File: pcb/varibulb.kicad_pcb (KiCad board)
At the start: 2 copper layers, 53.8 x 53.8 mm, 44 parts, among them IC1 ATTINY2313A-P, P1 MAINS LIVE, P2 MAINS LIVE, P3 LAMP 1, P4 LAMP 2, P5 MAINS GROUND, P6 ISP, P7 COMM, SW1 ENCODER, U1 TRIAC, U2 TRIAC, U3 LDO 5V, X1 10MHz

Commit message: arrange some components
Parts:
- R1, R2, R6: footprint Resistors_ThroughHole:Resistor_Horizontal_RM15mm -> Resistors_ThroughHole:Resistor_Horizontal_RM10mm
- U3: footprint Housings_TO-92:TO-92-Free-molded-narrow -> Housings_TO-92:TO-92-Free-molded-wide
- moved U2 139.0 mm to (61.7, 125.7), turned to 120 degrees
- moved D2 124.2 mm to (27.9, 80.5), turned to 45 degrees
- moved D4 102.5 mm to (50.3, 115.6), turned to 270 degrees
- moved P5 99.9 mm to (74.4, 145.0)
- moved R6 90.4 mm to (57.4, 128.0), turned to 300 degrees
- moved D5 84.3 mm to (47.0, 118.1), turned to 82 degrees
- moved R5 80.9 mm to (71.4, 133.6)
- moved D6 67.8 mm to (53.3, 115.6), turned to 270 degrees
- moved C1 67.5 mm to (84.6, 133.9), turned to 180 degrees
- moved D1 55.5 mm to (87.6, 122.2)
- moved C5 54.1 mm to (59.9, 114.8)
- moved D3 49.4 mm to (87.1, 126.7)
- moved R1 46.8 mm to (89.7, 135.6), turned to 55 degrees
- moved R2 46.3 mm to (81.8, 130.0), turned to 180 degrees
- moved R3 40.3 mm to (101.9, 119.4), turned to 270 degrees
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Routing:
- net GND: track 0.00 -> 61.4 mm
- net Net-(P4-Pad1): track 0.00 -> 21.0 mm
- net Net-(C5-Pad1): track 0.00 -> 17.5 mm
- net Net-(F1-Pad2): track 0.00 -> 16.7 mm
- net Net-(C3-Pad1): track 0.00 -> 16.0 mm
- net /SENSE: track 0.00 -> 14.3 mm
- net Net-(F1-Pad1): track 0.00 -> 12.5 mm
- net Net-(C3-Pad2): track 0.00 -> 10.5 mm
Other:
- net class Default: clearance 0.2 -> 0.1; trace_width 0.25 -> 0.8; via_dia 0.6 -> 2.2; via_drill 0.4 -> 0.8
- rule trace_clearance: 0.2 -> 0.1

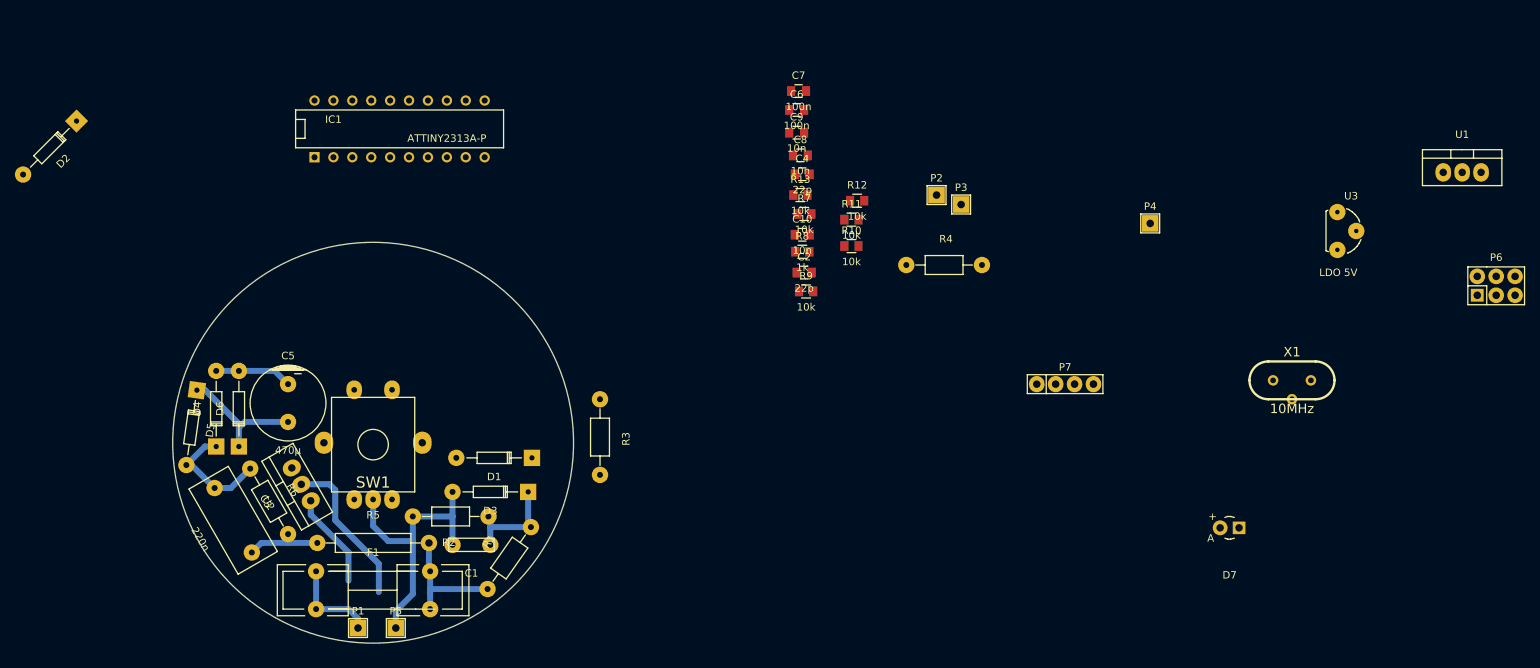
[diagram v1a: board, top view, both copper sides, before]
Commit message: arrange more components
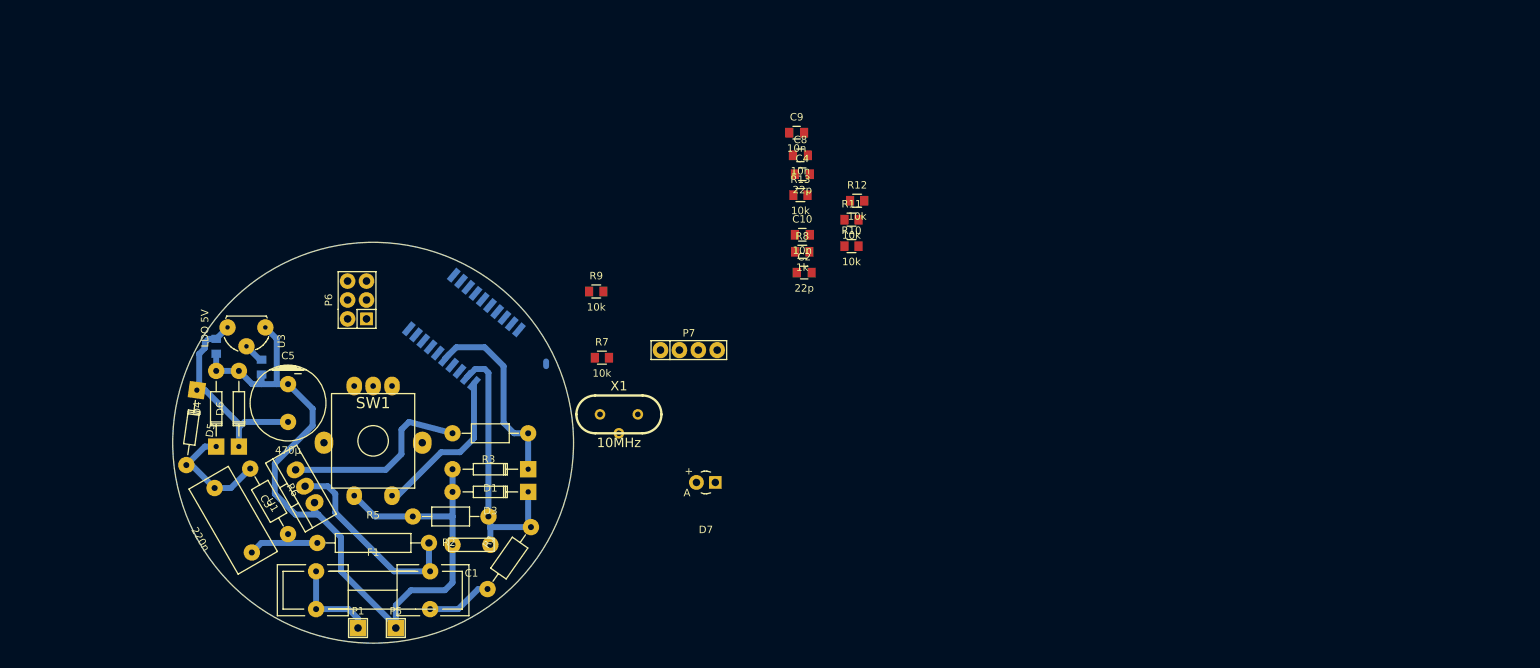
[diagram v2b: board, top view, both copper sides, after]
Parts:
- removed D2: 5v, Diodes_ThroughHole:Diode_DO-35_SOD27_Horizontal_RM10
- removed P2: MAINS LIVE, Pin_Headers:Pin_Header_Straight_1x01
- removed P3: LAMP 1, Pin_Headers:Pin_Header_Straight_1x01
- removed P4: LAMP 2, Pin_Headers:Pin_Header_Straight_1x01
- removed R4: 470Ω, Resistors_ThroughHole:Resistor_Horizontal_RM10mm
- removed U2: TRIAC, Transistors_TO-220:TO-220_Neutral123_Vertical
- C6, C7: moved to B.Cu
- IC1: value ATTINY2313A-P -> ATTINY2313A-S; footprint Sockets_DIP:DIP-20__300 -> Housings_SOIC:SOIC-20_7.5x12.8mm_Pitch1.27mm; moved to B.Cu
- moved U1 161.1 mm to (62.2, 126.0), turned to 120 degrees
- moved P6 153.0 mm to (69.2, 101.0), turned to 90 degrees
- moved U3 147.1 mm to (54.4, 104.6), turned to 270 degrees
- moved X1 90.5 mm to (104.4, 116.3)
- moved C6 84.2 mm to (50.3, 107.2), turned to 90 degrees
- moved C7 81.1 mm to (56.4, 110.0), turned to 90 degrees
- moved D7 70.6 mm to (116.1, 125.5)
- moved P7 50.8 mm to (113.8, 107.7)
- moved R7 33.3 mm to (102.1, 108.7)
- moved IC1 28.3 mm to (83.6, 104.9), turned to 230 degrees
- moved R9 28.2 mm to (101.3, 99.8)
- moved R3 14.7 mm to (87.1, 118.9), turned to 180 degrees
- moved D1 1.61 mm to (87.1, 123.7)
- turned SW1 to 180 degrees
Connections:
- IC1 pad 16: /SW2 -> (no net)
- U1 pad 2: Net-(P3-Pad1) -> Net-(F1-Pad2)
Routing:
- net GND: track 61.4 -> 110.8 mm
- net Net-(R3-Pad2): track 0.00 -> 26.9 mm
- net /SW1: track 0.00 -> 26.0 mm
- net /SENSE: track 14.3 -> 37.2 mm
- net Net-(C10-Pad1): track 0.00 -> 21.6 mm
- net Net-(P4-Pad1): track 21.0 -> 0.00 mm
- net Net-(F1-Pad2): track 16.7 -> 35.7 mm
- net Net-(C5-Pad1): track 17.5 -> 28.2 mm
- net VCC: track 0.00 -> 2.78 mm
- net (no net): track 0.00 -> 0.64 mm

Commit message: two PCBs
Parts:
- added P2: BOARD, Pin_Headers:Pin_Header_Straight_1x04, F.Cu at (57.8, 104.8)
- added P3: BOARD, Pin_Headers:Pin_Header_Straight_1x04, F.Cu at (116.8, 95.2)
- moved SW1 103.1 mm to (172.7, 101.0)
- moved U3 102.7 mm to (156.8, 111.1)
- moved C6 89.9 mm to (137.8, 127.6)
- moved P6 85.0 mm to (150.5, 125.7)
- moved C7 74.6 mm to (127.6, 132.1)
- moved C1 41.6 mm to (59.1, 101.0), turned to 0 degrees
- moved IC1 27.2 mm to (99.1, 82.5), turned to 180 degrees
- moved D1 24.5 mm to (65.4, 112.4)
- moved D3 22.7 mm to (65.4, 120.0)
- moved X1 22.0 mm to (126.4, 114.9)
- moved R2 21.4 mm to (65.4, 116.2)
- moved R1 19.1 mm to (78.7, 120.0), turned to 180 degrees
- moved U1 18.0 mm to (79.4, 131.4), turned to 0 degrees
- moved D4 13.7 mm to (53.3, 128.9)
- moved C3 13.5 mm to (66.0, 130.2), turned to 0 degrees
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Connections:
- C1 pad 1: /SENSE -> Net-(C1-Pad1)
- C1 pad 2: GND -> GNDREF
- C5 pad 2: GND -> GNDREF
- C6 pad 2: Net-(C5-Pad1) -> Net-(C6-Pad2)
- D1 pad 1: GND -> GNDREF
- D1 pad 2: /SW1 -> Net-(D1-Pad2)
- D3 pad 1: GND -> GNDREF
- D3 pad 2: /SENSE -> Net-(C1-Pad1)
- D4 pad 1: GND -> GNDREF
- D6 pad 1: GND -> GNDREF
- IC1 pad 15: /SW1 -> /PHASE
- P5 pad 1: GND -> GNDREF
- R1 pad 2: /SENSE -> Net-(C1-Pad1)
- R2 pad 1: /SENSE -> Net-(C1-Pad1)
- R2 pad 2: GND -> GNDREF
- R3 pad 1: /SW1 -> Net-(D1-Pad2)
- U1 pad 1: GND -> GNDREF
- U3 pad 3: Net-(C5-Pad1) -> Net-(C6-Pad2)
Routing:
- net GND: track 110.8 -> 0.00 mm
- net GNDREF: track 0.00 -> 69.4 mm
- net /SENSE: track 37.2 -> 0.00 mm
- net Net-(C1-Pad1): track 0.00 -> 34.4 mm
- net Net-(R3-Pad2): track 26.9 -> 0.00 mm
- net /SW1: track 26.0 -> 0.00 mm
- net Net-(C10-Pad1): track 21.6 -> 0.00 mm
- net Net-(F1-Pad2): track 35.7 -> 17.2 mm
- net Net-(D1-Pad2): track 0.00 -> 15.3 mm
- net Net-(C3-Pad2): track 10.5 -> 19.4 mm
- net Net-(C5-Pad1): track 28.2 -> 23.8 mm
- net Net-(C3-Pad1): track 16.0 -> 12.5 mm
- net VCC: track 2.78 -> 0.00 mm
- net (no net): track 0.64 -> 0.00 mm

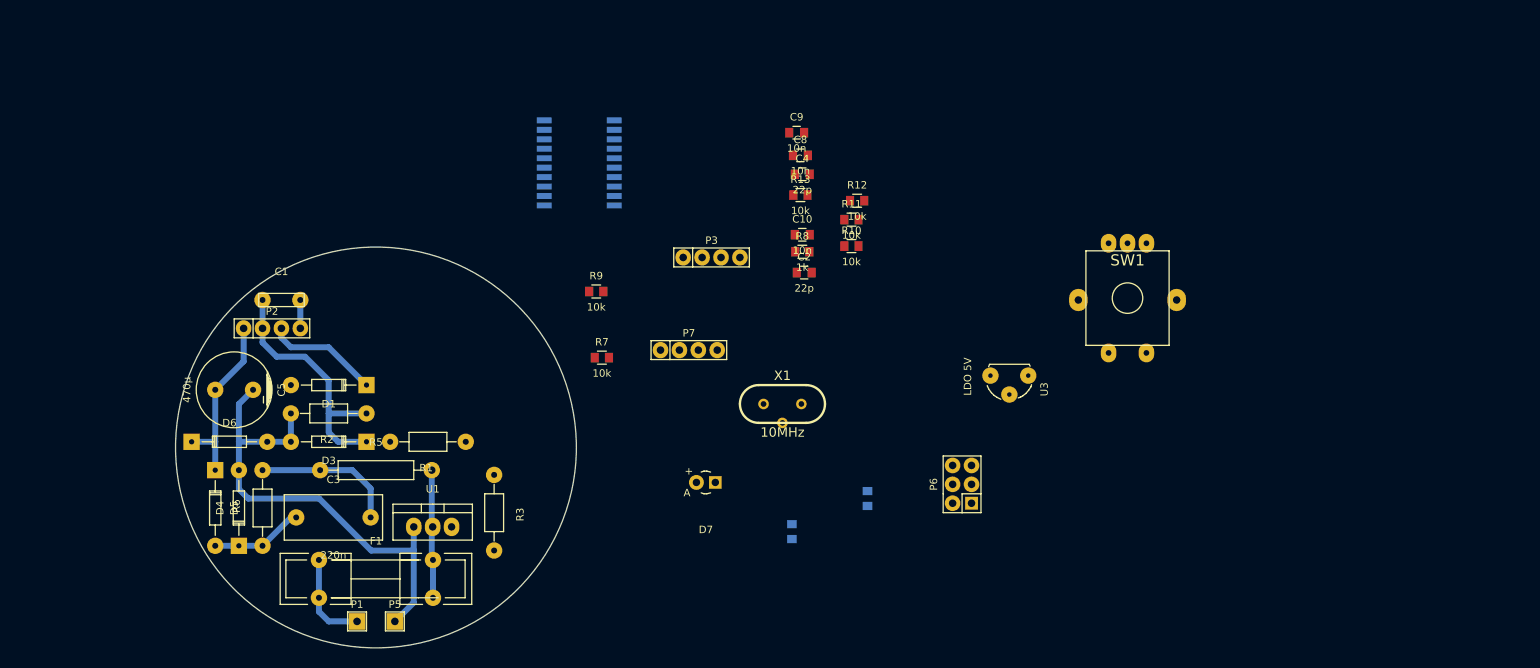
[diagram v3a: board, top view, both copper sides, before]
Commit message: arrange power pcb
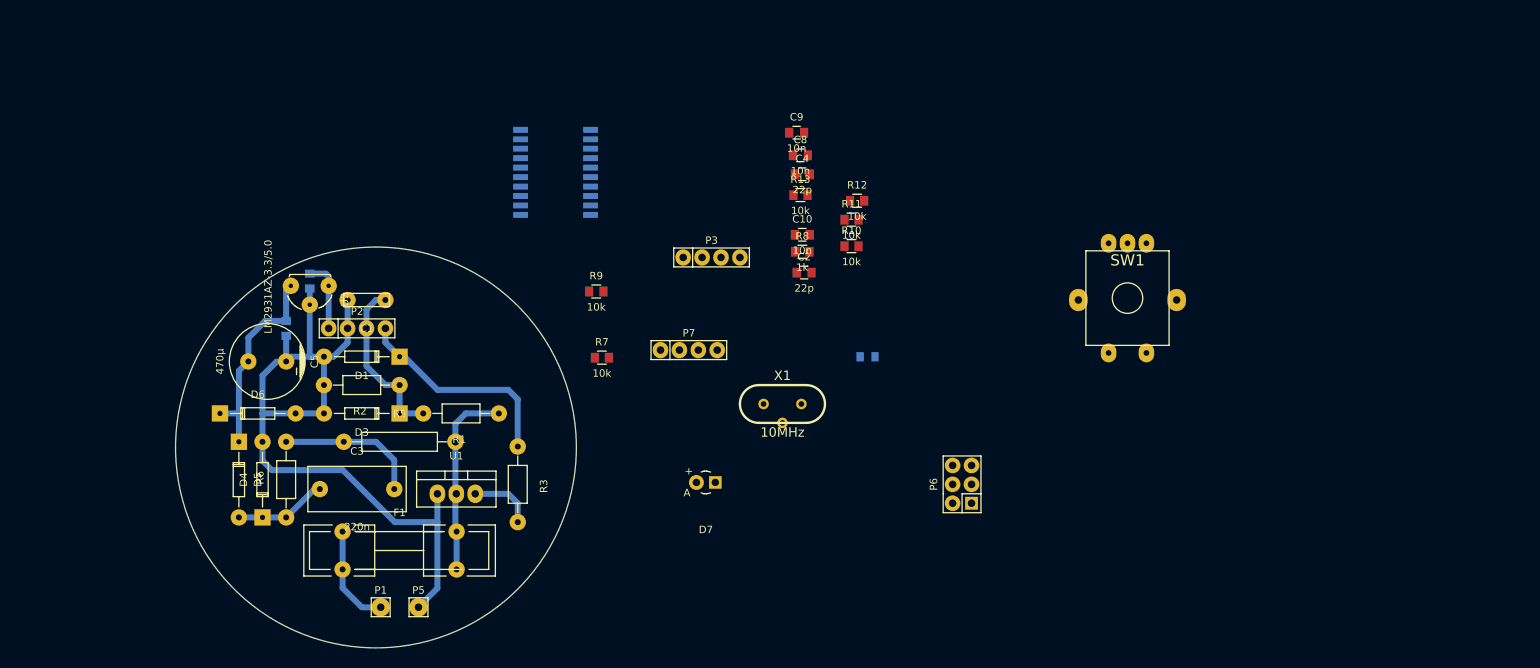
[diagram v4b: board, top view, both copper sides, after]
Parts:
- removed U3: LDO 5V, Housings_TO-92:TO-92-Free-molded-wide
- added C11: 100n, Capacitors_SMD:C_0805, B.Cu at (137.8, 108.6)
- added U2: LM2931AZ-3.3/5.0, Housings_TO-92:TO-92-Free-molded-wide, F.Cu at (62.9, 99.1)
- moved C6 81.4 mm to (59.7, 104.8)
- moved C7 73.0 mm to (62.9, 98.4)
- moved P2 11.4 mm to (69.2, 104.8)
- moved C1 11.4 mm to (70.5, 101.0), turned to 180 degrees
- moved R1 5.85 mm to (83.2, 116.2)
- moved C5 5.85 mm to (57.1, 109.2)
- moved D1 5.85 mm to (69.8, 108.6)
- moved D3 5.85 mm to (69.8, 116.2)
- moved R2 5.85 mm to (69.8, 112.4)
- moved U1 5.46 mm to (82.5, 127.0)
- moved D6 5.39 mm to (55.9, 116.2)
- moved C3 4.96 mm to (69.2, 126.4)
- moved F1 4.96 mm to (74.9, 134.6)
- moved R5 4.96 mm to (74.9, 120.0)
- moved D5 4.96 mm to (53.3, 125.1)
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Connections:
- C6 pad 1: GND -> GNDREF
- C6 pad 2: Net-(C6-Pad2) -> Net-(C5-Pad1)
- C7 pad 1: GND -> GNDREF
- C7 pad 2: VCC -> Net-(C7-Pad2)
- P2 pad 1: Net-(C5-Pad1) -> Net-(C7-Pad2)
- P2 pad 2: Net-(C1-Pad1) -> GNDREF
- P2 pad 3: Net-(D1-Pad2) -> Net-(C1-Pad1)
- P2 pad 4: GNDREF -> Net-(D1-Pad2)
- P3 pad 1: Net-(C6-Pad2) -> VCC
- P3 pad 2: /SENSE -> GND
- P3 pad 3: /PHASE -> /SENSE
- P3 pad 4: GND -> /PHASE
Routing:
- net GNDREF: track 69.4 -> 100.8 mm
- net Net-(D1-Pad2): track 15.3 -> 29.2 mm
- net Net-(C1-Pad1): track 34.4 -> 23.2 mm
- net Net-(C7-Pad2): track 0.00 -> 9.68 mm
- net Net-(F1-Pad2): track 17.2 -> 26.0 mm
- net Net-(R3-Pad2): track 0.00 -> 8.78 mm
- net Net-(C5-Pad1): track 23.8 -> 28.0 mm
- net Net-(F1-Pad1): track 12.6 -> 13.8 mm

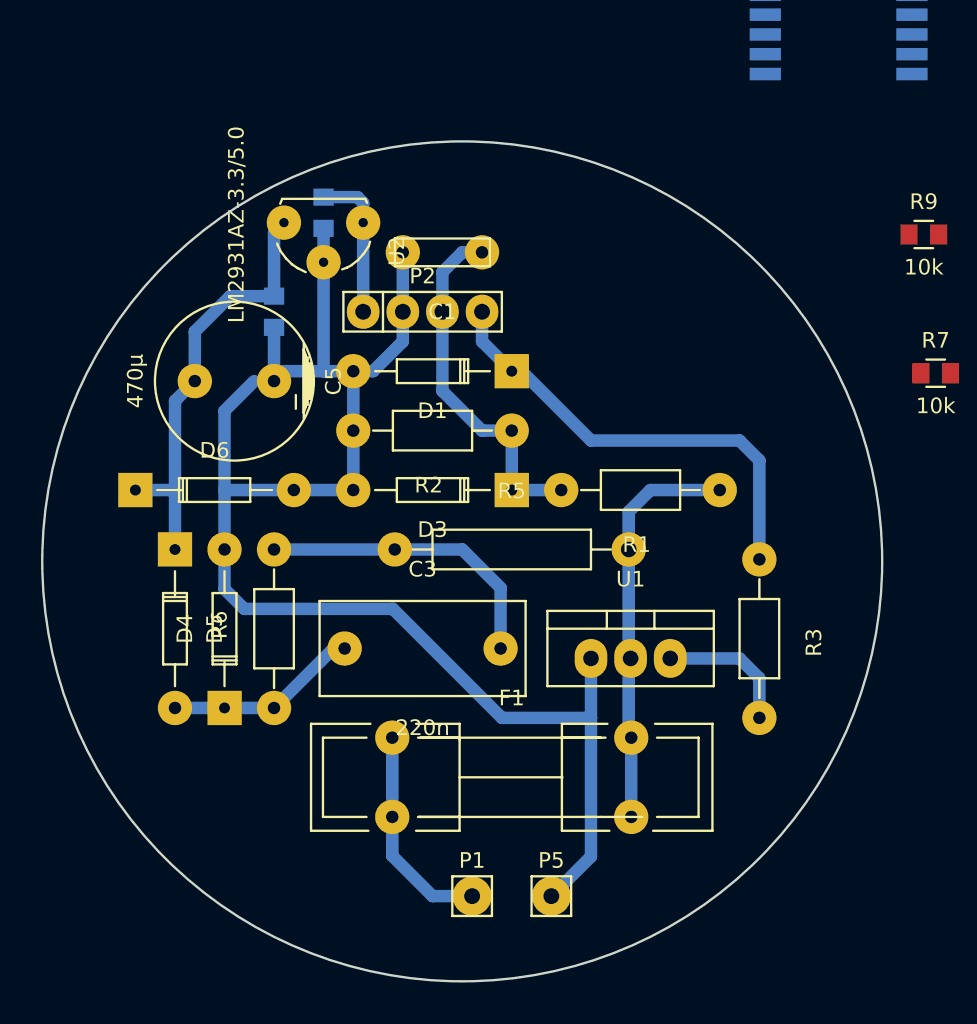
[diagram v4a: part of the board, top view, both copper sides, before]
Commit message: set appropriate track widths
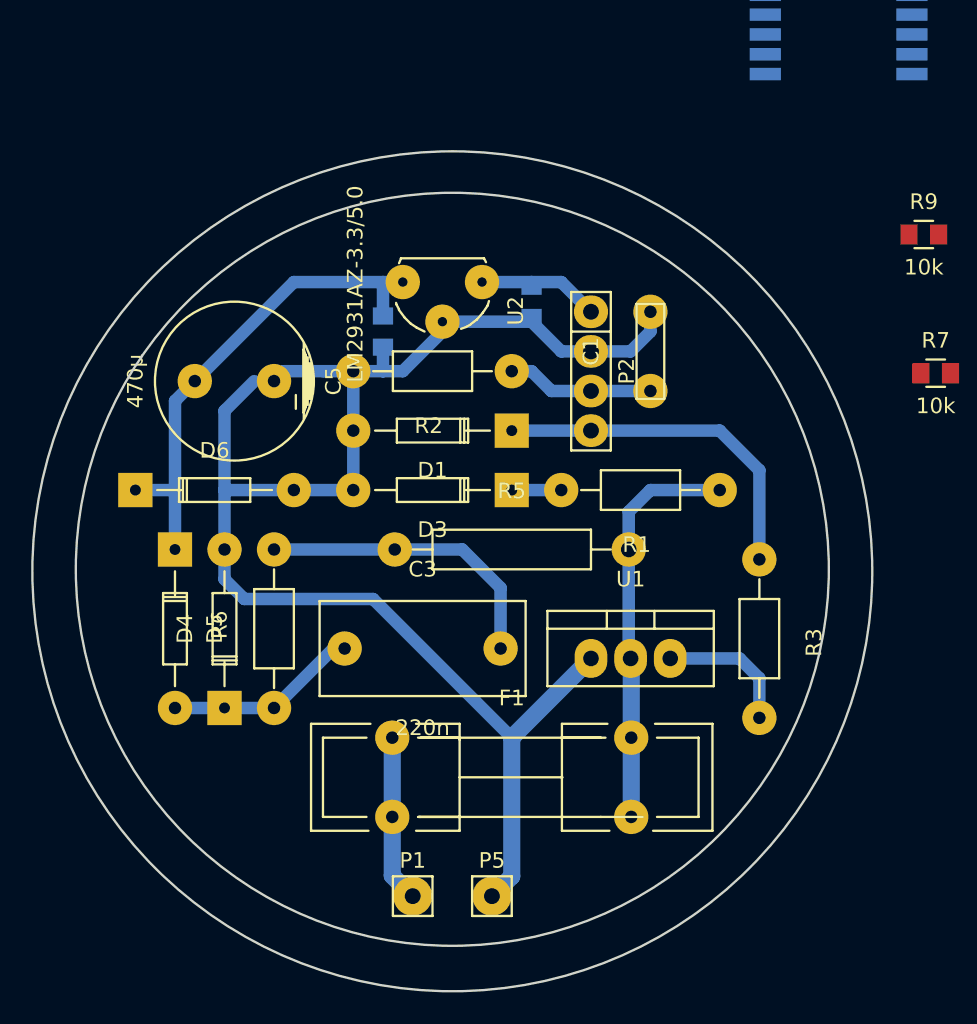
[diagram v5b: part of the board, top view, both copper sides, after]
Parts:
- moved C1 14.8 mm to (83.8, 107.3), turned to 90 degrees
- moved C7 14.5 mm to (76.2, 104.1)
- moved P2 11.4 mm to (80.0, 108.6), turned to 270 degrees
- moved U2 8.52 mm to (70.5, 102.9)
- moved C6 7.10 mm to (66.7, 106.0)
- moved D1 3.81 mm to (69.8, 112.4)
- moved P1 3.81 mm to (68.6, 142.2)
- moved P5 3.81 mm to (73.7, 142.2)
- moved R2 3.81 mm to (69.8, 108.6)
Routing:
- net Net-(C1-Pad1): track 23.2 -> 13.2 mm
- net Net-(D1-Pad2): track 29.2 -> 22.6 mm
- net Net-(C5-Pad1): track 28.0 -> 32.0 mm
- net Net-(F1-Pad1): track 13.8 -> 10.7 mm
- net Net-(C7-Pad2): track 9.68 -> 8.04 mm
- net GNDREF: track 100.8 -> 99.7 mm
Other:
- outline, holes or cut-outs redrawn
